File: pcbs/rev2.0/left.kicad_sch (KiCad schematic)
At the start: 32 parts, among them J1 Conn_ST_STDC14, SW65 MK-12C03-G015, U1 LDI1117, U2 USBLC6-2SC6_C5261088, U3 358, U4 STM32F446RCTx, U5 GT-TC020A-H035-L05, Y1 8MHz

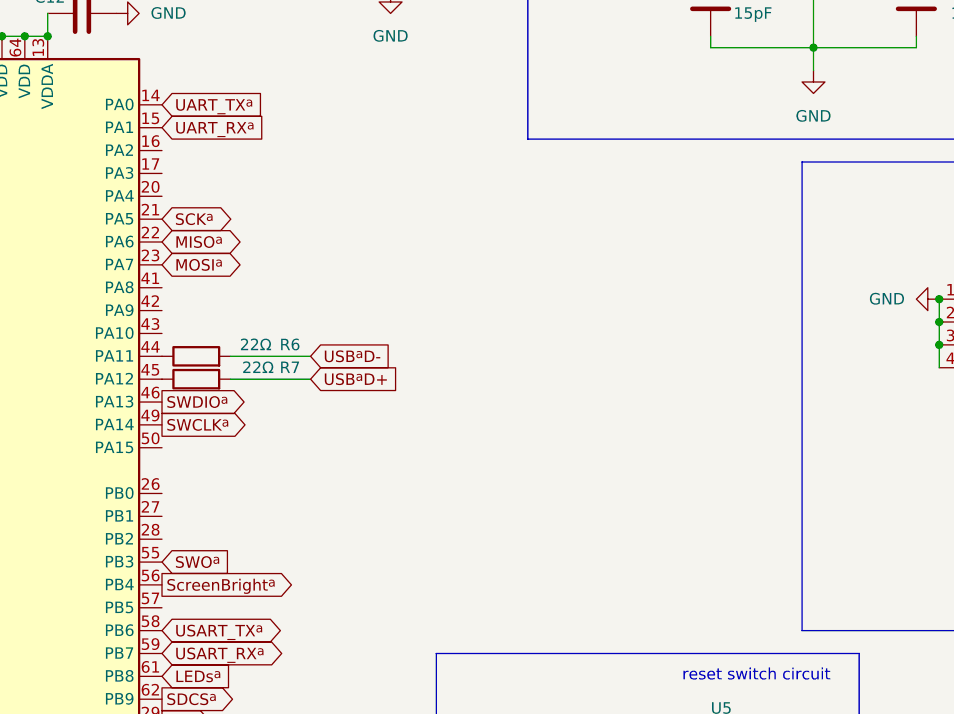
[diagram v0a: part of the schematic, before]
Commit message: Finish Layout for Master Half.
- Unimplemented handedness yet.
- Rest of the board should be working already
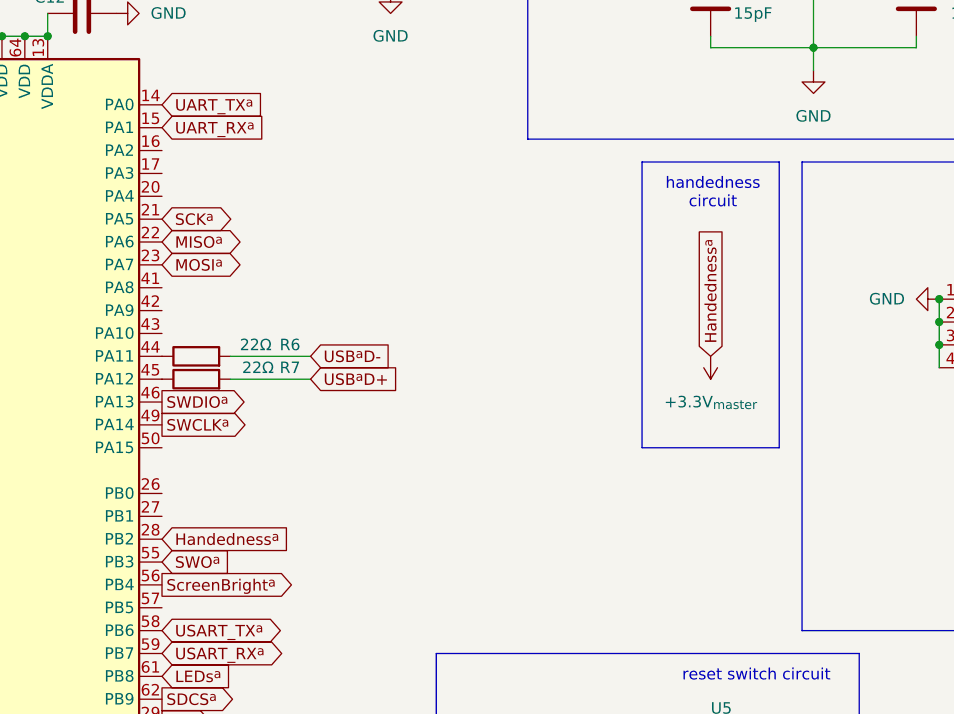
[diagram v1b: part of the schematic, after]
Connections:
- net +3.3V_{master}: now also U4.28 (PB2)
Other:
- note added: "handedness circuit"
- company: (none) -> Afonso Lopo
- title: (none) -> Migrane - Master Half
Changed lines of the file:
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@@
 	(generator_version "9.0")
 	(paper "A4")
+	(title_block
+		(title "Migrane - Master Half")
+		(rev "3.0")
+		(company "Afonso Lopo")
+	)
 	(rectangle
 		(start 138.43 73.66)
@@
 	)
 	(rectangle
+		(start 151.13 110.49)
+		(end 166.37 142.24)
+		(stroke
+			(width 0)
+			(type default)
+		)
+		(fill
+			(type none)
+		)
+	)
+	(rectangle
 		(start 13.97 13.97)
 		(end 120.65 68.58)
@@
 		)
 	)
+	(text "handedness\ncircuit"
+		(exclude_from_sim no)
+		(at 159.004 114.046 0)
+		(effects
+			(font
+				(size 1.27 1.27)
+			)
+		)
+	)
 	(text "reset switch circuit\n"
 		(exclude_from_sim no)
@@
 		)
 	)
+	(global_label "Handedness^{a}"
+		(shape input)
+		(at 158.75 132.08 90)
+		(fields_autoplaced yes)
+		(effects
+			(font
+				(size 1.27 1.27)
+			)
+			(justify left)
+		)
+		(property "Intersheetrefs" "${INTERSHEET_REFS}"
+			(at 158.75 116.8159 90)
+			(effects
+				(font
+					(size 1.27 1.27)
+				)
+				(justify left)
+				(hide yes)
+			)
+		)
+	)
 	(global_label "USART_TX^{a}"
 		(shape bidirectional)
@@
 		)
 	)
+	(global_label "Handedness^{a}"
+		(shape input)
+		(at 97.79 152.4 0)
+		(fields_autoplaced yes)
+		(effects
+			(font
+				(size 1.27 1.27)
+			)
+			(justify left)
+		)
+		(property "Intersheetrefs" "${INTERSHEET_REFS}"
+			(at 113.0541 152.4 0)
+			(effects
+				(font
+					(size 1.27 1.27)
+				)
+				(justify left)
+				(hide yes)
+			)
+		)
+	)
 	(global_label "MOSI^{a}"
 		(shape bidirectional)
@@
 					(unit 1)
 				)
+			)
+		)
+	)
+	(symbol
+		(lib_id "power:+3.3V")
+		(at 158.75 132.08 180)
+		(unit 1)
+		(exclude_from_sim no)
+		(in_bom yes)
+		(on_board yes)
+		(dnp no)
+		(fields_autoplaced yes)
+		(property "Reference" "#PWR012"
+			(at 158.75 128.27 0)
+			(effects
+				(font
+					(size 1.27 1.27)
+				)
+				(hide yes)
+			)
+		)
+		(property "Value" "+3.3V_{master}"
+			(at 158.75 137.16 0)
+			(effects
+				(font
+					(size 1.27 1.27)
+				)
+			)
+		)
+		(property "Footprint" ""
+			(at 158.75 132.08 0)
+			(effects
+				(font
+					(size 1.27 1.27)
+				)
+				(hide yes)
+			)
+		)
+		(property "Datasheet" ""
+			(at 158.75 132.08 0)
+			(effects
+				(font
+					(size 1.27 1.27)
+				)
+				(hide yes)
+			)
+		)
+		(property "Description" "Power symbol creates a global label with name \"+3.3V\""
+			(at 158.75 132.08 0)
+			(effects
+				(font
+					(size 1.27 1.27)
+				)
+				(hide yes)
+			)
+		)
+		(pin "1"
+		)
+		(instances
+			(project ""
+				(path "/4f8ca79b-a6b7-44ba-9756-90741cca88f0/15f746c7-5e4f-47a6-8468-51b5a4a1d3d2"
+					(reference "#PWR012")
+					(unit 1)
+				)

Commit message: ongoing work
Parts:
- removed D66: GLED, easyeda2kicad:LED0805-R-RD, symbol Device:LED
- removed D67: YLED, easyeda2kicad:LED0805-R-RD, symbol Device:LED
